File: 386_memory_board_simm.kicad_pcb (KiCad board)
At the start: 4 copper layers, 222.2 x 85.7 mm, 75 parts, among them J1 Bus_386_Memory, M3 MountingHole_3.2mm_M3_DIN965, U10 74LS174, U11 74LS174, U12 74LS174, U13 74LS174, U14 74LS158, U15 74LS158, U16 74LS158, U17 7410, U18 SPARE, U19 SPARE, U20 DS1010, U22 DS1010, U37 7410, U38 7400, U39 7400, U40 7410, U43 74LS02, U44 7410, U45 74LS04, U5 74LS174, U6 74LS174, U7 74LS158, U8 74LS158, U9 74LS158

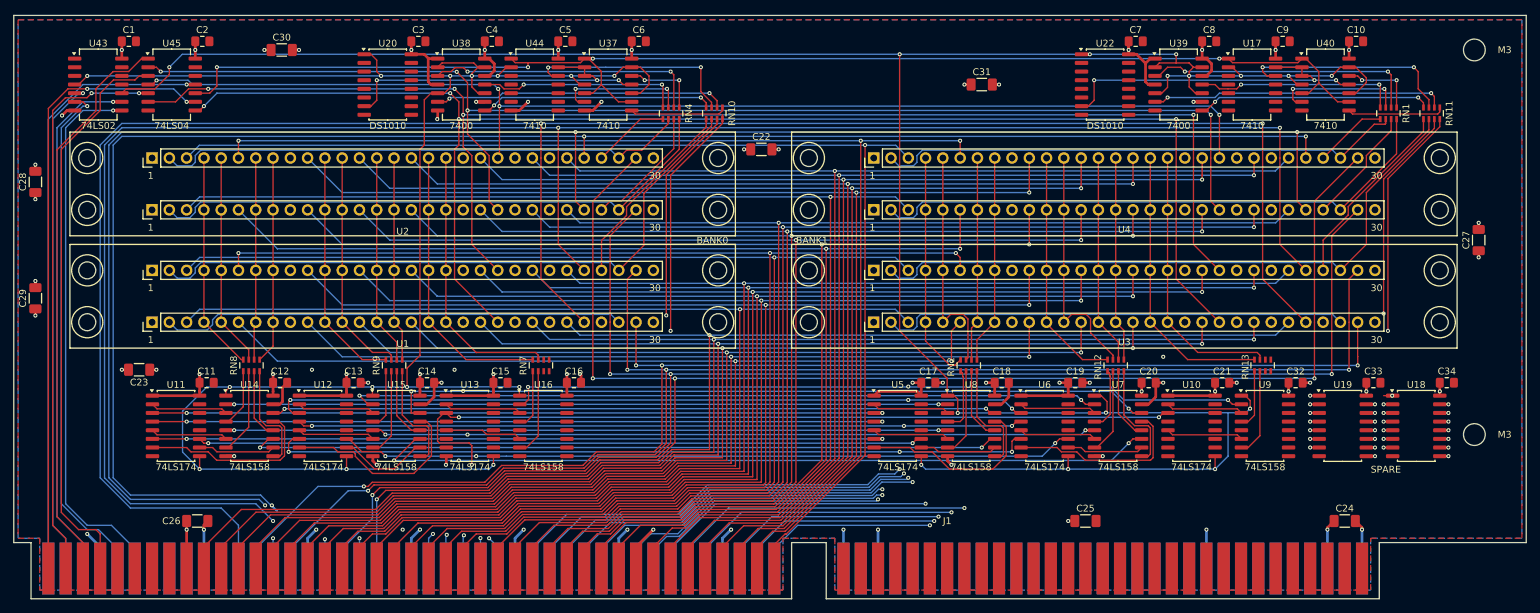
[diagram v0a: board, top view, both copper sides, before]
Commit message: fixed footprint of delay lines
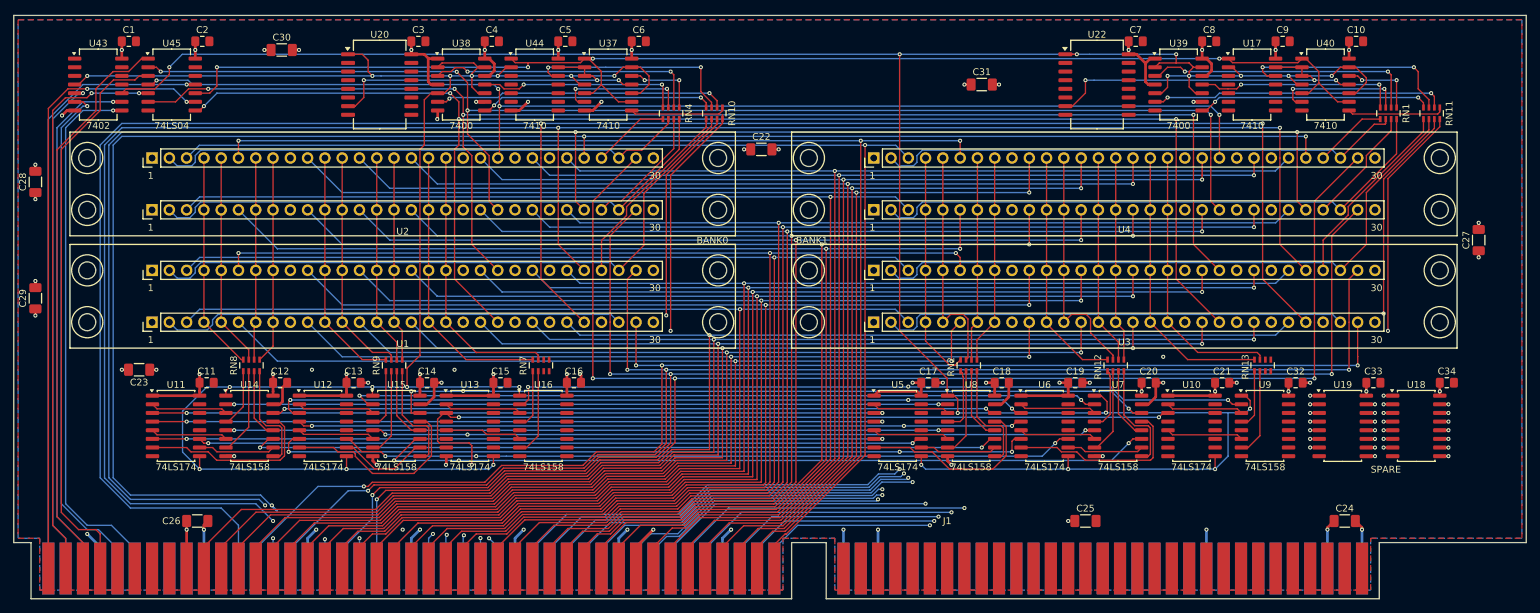
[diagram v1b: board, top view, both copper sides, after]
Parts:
- removed M3 (x2): MountingHole_3.2mm_M3_DIN965, MountingHole:MountingHole_3.2mm_M3_DIN965
- U20, U22: value DS1010 -> ~; footprint Package_SO:SO-16_5.3x10.2mm_P1.27mm -> Package_SO:SOIC-16W_7.5x12.8mm_P1.27mm
- U43: value 74LS02 -> 7402
- moved U20 1.19 mm to (216.3, 149.9)
- moved U22 1.19 mm to (321.7, 149.9)
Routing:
- net Net-(U20-TAP8): track 50.1 -> 52.3 mm
- net Net-(U22-TAP8): track 50.1 -> 51.9 mm
- net UNKN5: track 276.7 -> 277.8 mm

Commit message: added bracket mounting holes
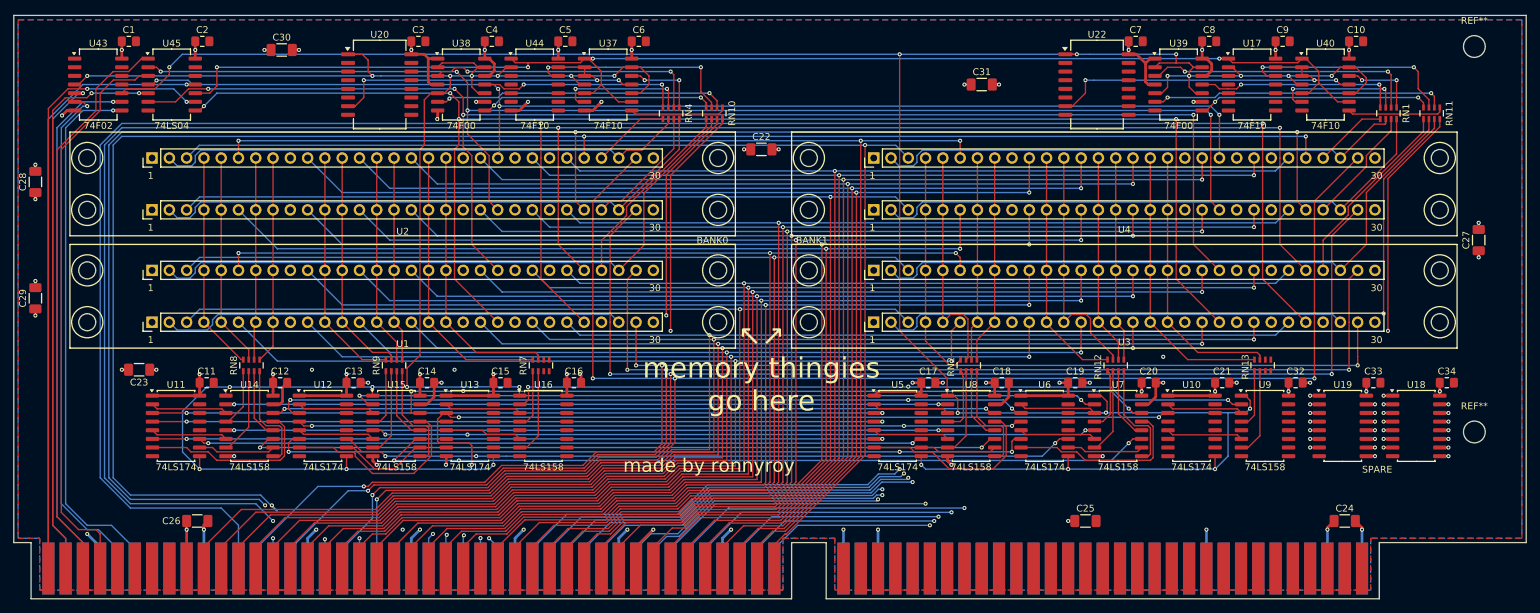
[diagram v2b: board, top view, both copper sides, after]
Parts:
- added G***: LOGO, 386_memory_board:i386_compatible_30mm, B.Cu at (275.0, 200.7)
- added REF**: MountingHole_3.2mm_M3_DIN965, MountingHole:MountingHole_3.2mm_M3_DIN965, F.Cu at (377.2, 200.9)
- added REF**: MountingHole_3.2mm_M3_DIN965, MountingHole:MountingHole_3.2mm_M3_DIN965, F.Cu at (377.2, 144.3)
- U17, U37, U40, U44: value 7410 -> 74F10
- U38, U39: value 7400 -> 74F00
- U43: value 7402 -> 74F02
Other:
- board text added: "made by ronnyroy"
- board text added: "↖↗ memory thingies go here"
